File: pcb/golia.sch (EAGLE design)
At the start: 23 parts, among them IC1 xm64a4u, U1 MCP1825S-3302E/DB, X2 EXT

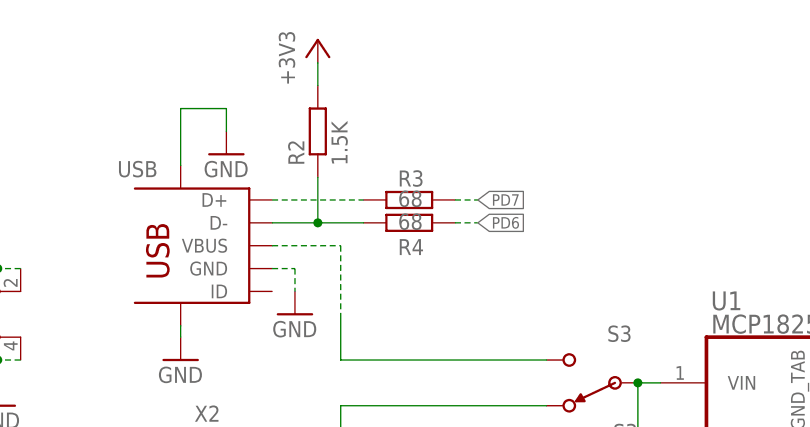
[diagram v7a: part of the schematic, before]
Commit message: Reduced width to 42mm, removed USB series resistors
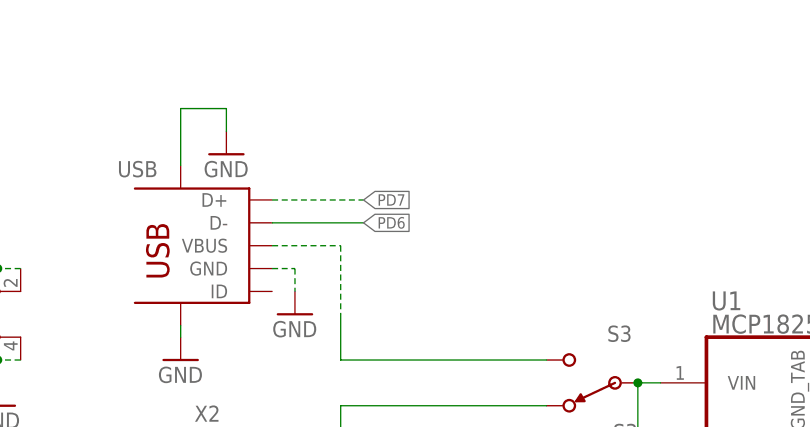
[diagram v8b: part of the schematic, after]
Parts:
- removed R2: 1.5K, rcl:R-EU_R0603
- removed R3, R4: 68, rcl:R-EU_R0603
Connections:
- removed net N$3: R2.1, R4.1, USB.D-
- removed net N$4: R3.1, USB.D+
- net +3V3: no longer R2.2
- net PD6: now also USB.D-; no longer R4.2
- net PD7: now also USB.D+; no longer R3.2
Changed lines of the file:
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@@
 <part name="GND4" library="supply1" deviceset="GND" device=""/>
 <part name="GND6" library="supply1" deviceset="GND" device=""/>
-<part name="+3V5" library="supply1" deviceset="+3V3" device=""/>
 <part name="GND7" library="supply1" deviceset="GND" device=""/>
 <part name="X2" library="Connectors" deviceset="JST-2" device="2MM-PTH-VERT-LOCK" value="EXT"/>
@@
 <part name="C1" library="Passives" deviceset="C" device="0603" value="10u"/>
 <part name="C2" library="rcl" deviceset="C-EU" device="C1206" value="100u"/>
-<part name="R2" library="rcl" deviceset="R-EU_" device="R0603" value="1.5K"/>
-<part name="R3" library="rcl" deviceset="R-EU_" device="R0603" value="68"/>
-<part name="R4" library="rcl" deviceset="R-EU_" device="R0603" value="68"/>
 <part name="S3" library="Switches" deviceset="SPDT" device="EG-1218" value="S3"/>
 <part name="USB" library="Connectors" deviceset="USB-MINI" device="B-PTH"/>
@@
 <instance part="GND4" gate="1" x="139.7" y="-5.08"/>
 <instance part="GND6" gate="1" x="160.02" y="58.42"/>
-<instance part="+3V5" gate="G$1" x="162.56" y="88.9"/>
 <instance part="GND7" gate="1" x="165.1" y="35.56"/>
 <instance part="X2" gate="G$1" x="152.4" y="41.91"/>
@@
 <instance part="C1" gate="G$1" x="198.12" y="38.1"/>
 <instance part="C2" gate="G$1" x="236.22" y="38.1"/>
-<instance part="R2" gate="G$1" x="162.56" y="78.74" rot="R90"/>
-<instance part="R3" gate="G$1" x="172.72" y="71.12" smashed="yes">
-<attribute name="NAME" x="171.45" y="72.6186" size="1.778" layer="95"/>
-<attribute name="VALUE" x="171.45" y="70.358" size="1.778" layer="96"/>
-</instance>
-<instance part="R4" gate="G$1" x="172.72" y="68.58" smashed="yes">
-<attribute name="NAME" x="171.45" y="64.9986" size="1.778" layer="95"/>
-<attribute name="VALUE" x="171.45" y="67.818" size="1.778" layer="96"/>
-</instance>
 <instance part="S3" gate="G$1" x="193.04" y="50.8" rot="R180"/>
 <instance part="USB" gate="G$1" x="152.4" y="66.04" smashed="yes" rot="MR0">
@@
 </segment>
 <segment>
-<pinref part="+3V5" gate="G$1" pin="+3V3"/>
-<wire x1="162.56" y1="86.36" x2="162.56" y2="83.82" width="0.1524" layer="91"/>
-<pinref part="R2" gate="G$1" pin="2"/>
-</segment>
-<segment>
 <wire x1="233.68" y1="50.8" x2="236.22" y2="50.8" width="0.1524" layer="91"/>
 <wire x1="236.22" y1="50.8" x2="236.22" y2="55.88" width="0.1524" layer="91"/>
@@
 </segment>
 <segment>
-<wire x1="177.8" y1="68.58" x2="180.34" y2="68.58" width="0.1524" layer="91" style="longdash"/>
-<label x="180.34" y="68.58" size="1.27" layer="95" xref="yes"/>
-<pinref part="R4" gate="G$1" pin="2"/>
+<label x="167.64" y="68.58" size="1.27" layer="95" xref="yes"/>
+<pinref part="USB" gate="G$1" pin="D-"/>
+<wire x1="167.64" y1="68.58" x2="157.48" y2="68.58" width="0.1524" layer="91"/>
 </segment>
 </net>
@@
 </segment>
 <segment>
-<wire x1="177.8" y1="71.12" x2="180.34" y2="71.12" width="0.1524" layer="91" style="longdash"/>
-<label x="180.34" y="71.12" size="1.27" layer="95" xref="yes"/>
-<pinref part="R3" gate="G$1" pin="2"/>
+<label x="167.64" y="71.12" size="1.27" layer="95" xref="yes"/>
+<wire x1="157.48" y1="71.12" x2="167.64" y2="71.12" width="0.1524" layer="91" style="longdash"/>
+<pinref part="USB" gate="G$1" pin="D+"/>
 </segment>
 </net>
@@
 </segment>
 </net>
-<net name="N$4" class="0">
-<segment>
-<wire x1="157.48" y1="71.12" x2="167.64" y2="71.12" width="0.1524" layer="91" style="longdash"/>
-<pinref part="R3" gate="G$1" pin="1"/>
-<pinref part="USB" gate="G$1" pin="D+"/>
-</segment>
-</net>
 <net name="N$1" class="0">
 <segment>
@@
 </segment>
 </net>
-<net name="N$3" class="0">
-<segment>
-<wire x1="157.48" y1="68.58" x2="162.56" y2="68.58" width="0.1524" layer="91"/>
-<wire x1="167.64" y1="68.58" x2="162.56" y2="68.58" width="0.1524" layer="91"/>
-<wire x1="162.56" y1="73.66" x2="162.56" y2="68.58" width="0.1524" layer="91"/>
-<junction x="162.56" y="68.58"/>
-<pinref part="R2" gate="G$1" pin="1"/>
-<pinref part="R4" gate="G$1" pin="1"/>
-<pinref part="USB" gate="G$1" pin="D-"/>
-</segment>
-</net>
